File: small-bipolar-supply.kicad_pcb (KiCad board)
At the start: 2 copper layers, 25.9 x 25 mm, 23 parts, among them J1 USB_C_Receptacle_PowerOnly_6P, J10 Conn_01x01, J2 Conn_01x02, J3 Conn_01x02, J4 Conn_01x02, J7 Conn_01x02, J8 Conn_01x02, J9 Conn_01x01, U1 LM2776

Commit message: trace layout complete
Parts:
- moved L2 0.85 mm to (99.6, 62.7)
- moved C3 0.05 mm to (90.6, 63.1)
- turned JP1 to 180 degrees
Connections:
- net Net-(U1-C1+) renamed /C+
- net Net-(U1-C1-) renamed /C-
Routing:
- net GND: track 0.00 -> 56.0 mm, vias 0 -> 10
- net /EN: track 0.00 -> 43.7 mm
- net VBUS: track 0.00 -> 30.2 mm
- net +5V: track 0.00 -> 14.2 mm
- net -5V: track 0.00 -> 13.4 mm
- net /VOUT: track 0.00 -> 9.56 mm
- net Net-(J1-CC2): track 0.00 -> 8.86 mm
- net Net-(J1-CC1): track 0.00 -> 8.83 mm
- net /C+: track 0.00 -> 2.51 mm
- net /C-: track 0.00 -> 2.41 mm

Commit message: branding and final tweaks
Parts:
- added G***: LOGO, small-bipolar-supply:polar, B.Cu at (100.8, 62.8)
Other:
- board text added: "William Tomlinson 2026 Simple-Bipolar-Supply"

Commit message: feat: new module symbol and footprints
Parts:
- added G***: LOGO, small-bipolar-supply:polar, B.Cu at (101.7, 62.2)

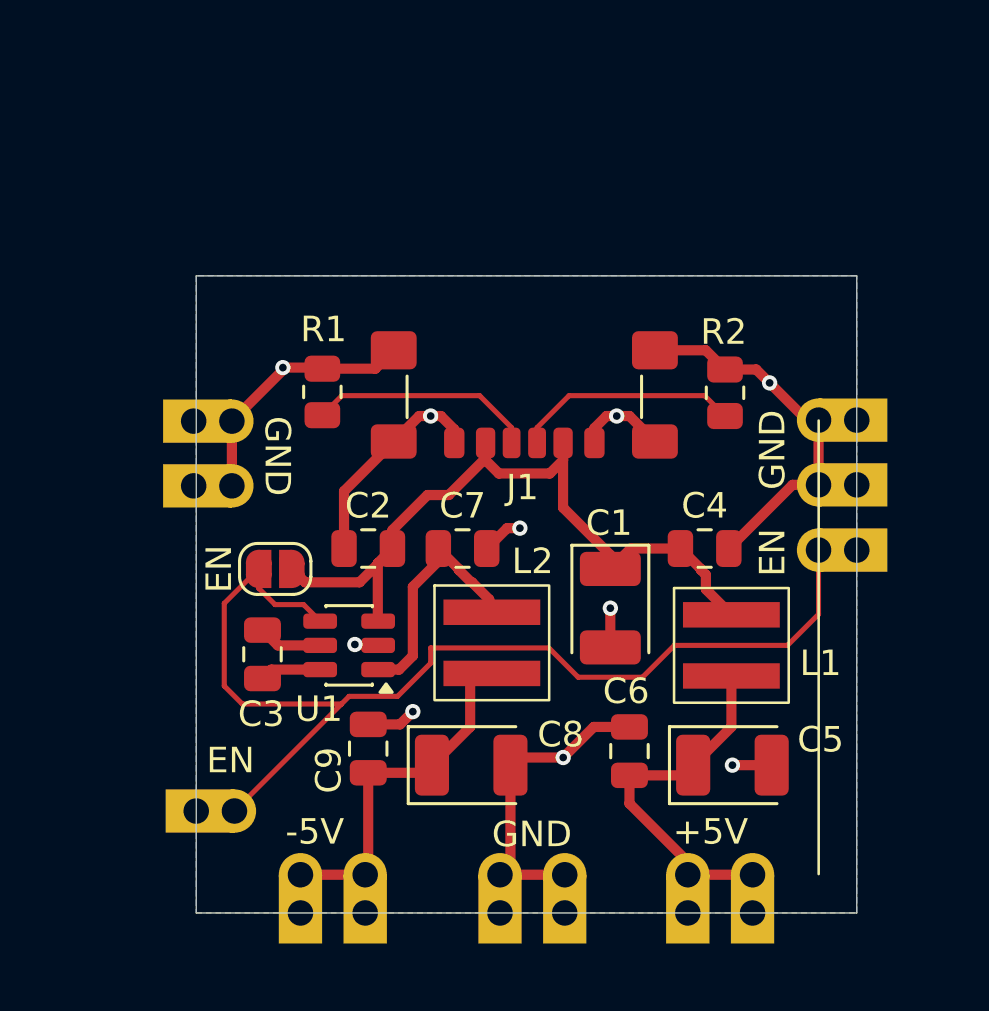
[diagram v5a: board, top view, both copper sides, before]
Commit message: Removed castellated edges & various layout tweaks
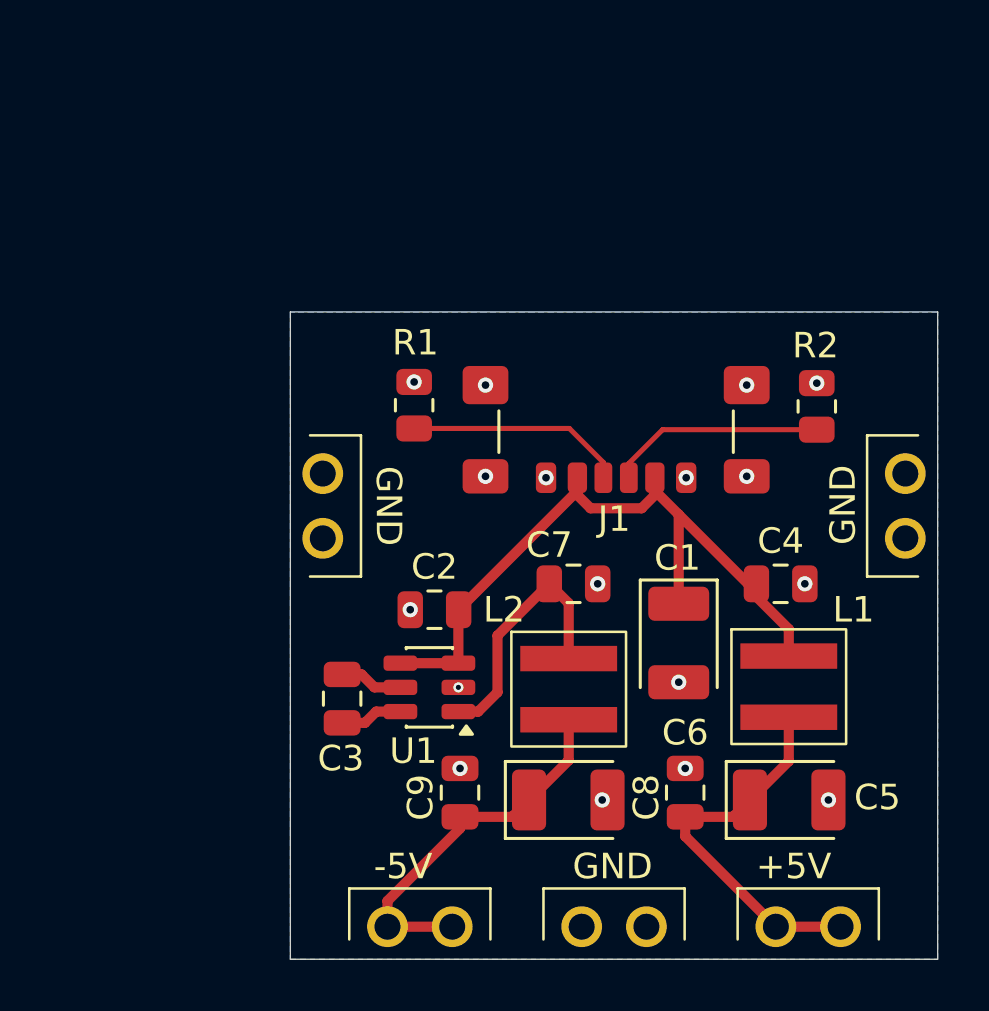
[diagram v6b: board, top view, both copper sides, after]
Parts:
- removed J10, J9: Conn_01x01, small-bipolar-supply:castellated_1_P2.54mm
- removed J2, J3, J4, J7, J8: Conn_01x02, small-bipolar-supply:castellated_2_P2.54mm
- removed JP1: SolderJumper_2_Open, Jumper:SolderJumper-2_P1.3mm_Open_RoundedPad1.0x1.5mm
- added U2: module_connectors, small-bipolar-supply:module-footprint, F.Cu at (93.0, 56.1)
- moved G*** 39.0 mm to (139.7, 61.0)
- moved G*** 39.0 mm to (140.6, 60.4)
- moved C7 4.57 mm to (102.8, 60.4)
- moved C8 4.05 mm to (102.6, 68.9)
- moved C9 3.99 mm to (98.4, 68.6)
- moved J1 3.85 mm to (104.5, 53.2)
- moved R2 3.64 mm to (112.4, 53.4)
- moved R1 3.64 mm to (96.6, 53.4)
- moved C3 3.58 mm to (93.7, 64.9)
- moved U1 3.55 mm to (97.1, 64.4)
- moved C2 3.54 mm to (97.3, 61.4)
- moved L2 3.52 mm to (102.6, 64.5)
- moved C4 3.29 mm to (110.9, 60.4)
- moved C1 3.01 mm to (106.9, 62.7)
- moved L1 2.77 mm to (111.3, 64.4)
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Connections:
- U1 pad 4: /EN -> VBUS
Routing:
- net GND: track 56.0 -> 0.00 mm, vias 10 -> 17
- net /EN: track 43.7 -> 0.00 mm
- net -5V: track 13.4 -> 14.8 mm
- net +5V: track 14.2 -> 15.3 mm
- net VBUS: track 30.2 -> 29.2 mm
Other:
- board size 25.9 x 25 mm -> 25.4 x 25.4 mm
- board text removed: "+5V"
- board text removed: "-5V"
- board text removed: "EN"
- board text removed: "GND"
